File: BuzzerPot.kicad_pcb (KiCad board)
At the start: 2 copper layers, 29.9 x 15.1 mm, 9 parts, among them J1 ConnM_01x03_Horizontal_2.54mm, Q2 AO3400_C4748804

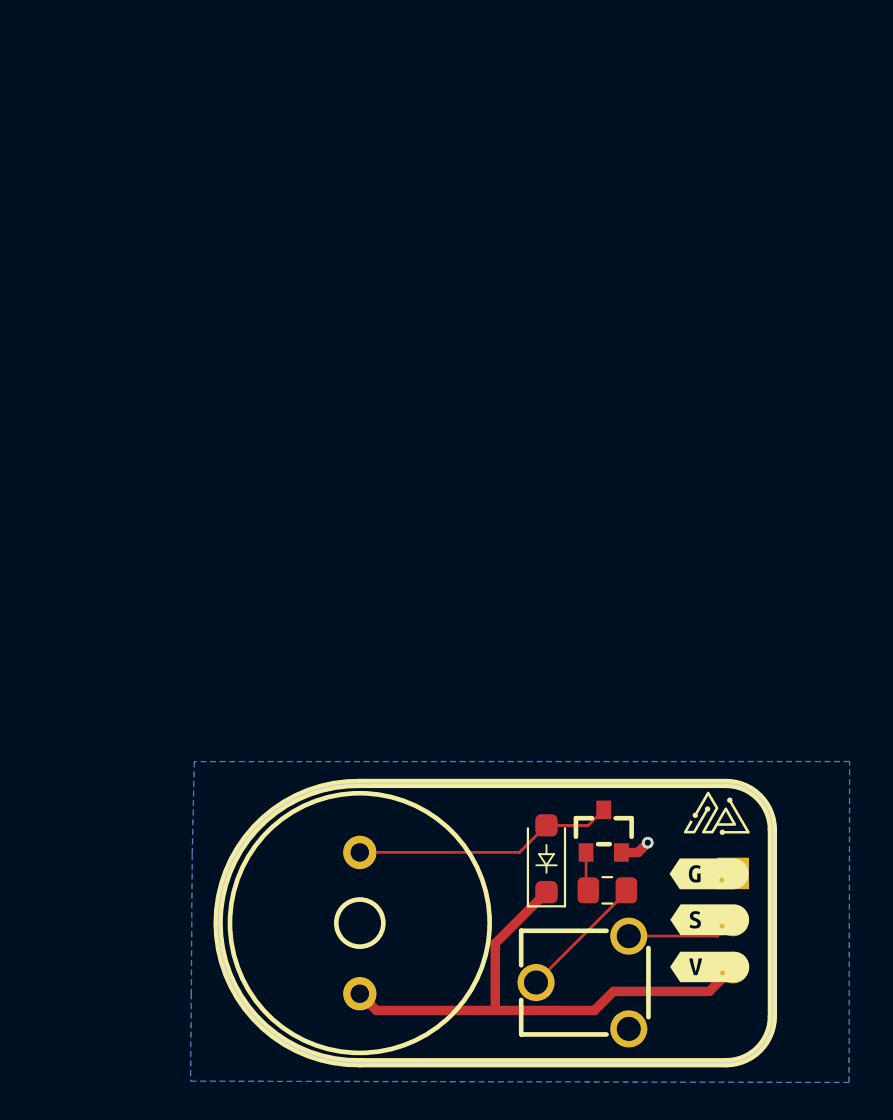
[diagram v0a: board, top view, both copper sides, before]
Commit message: Updated: Replaced Buzzer with Speaker
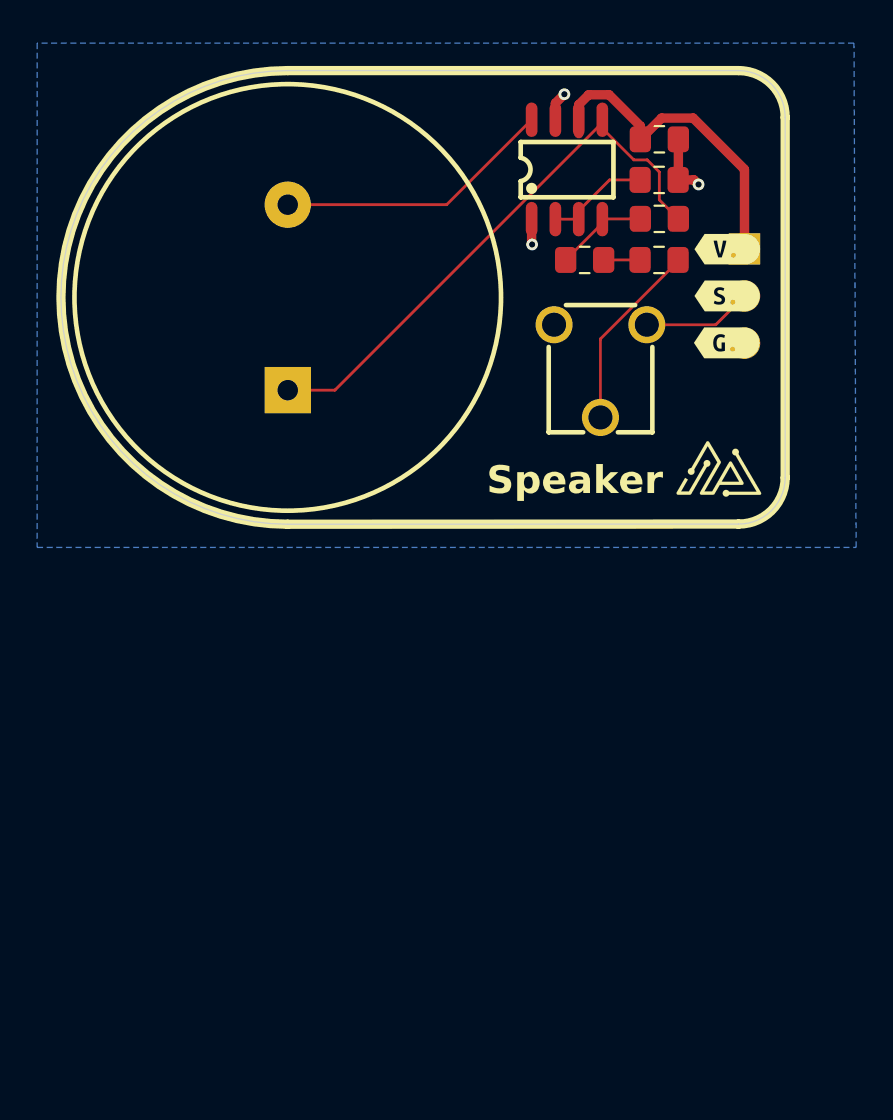
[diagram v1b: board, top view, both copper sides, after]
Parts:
- removed BUZZER2: SFN-1407PA7.6, easyeda2kicad:BUZ-TH_BD14.0-P7.60-D0.7
- removed D1: D_Schottky_SOD-123_xxV_xxA, Remal_KiCadLib:D_SOD-123
- removed Q2: AO3400_C4748804, easyeda2kicad:SOT-23_L2.9-W1.3-P1.90-LS2.4-BR
- removed kibuzzard-67C9871B: G***, kibuzzard-67C9871B
- removed kibuzzard-67C9872F: G***, kibuzzard-67C9872F
- removed kibuzzard-67C98740: G***, kibuzzard-67C98740
- added C1: 1uF, Remal_KiCadLib:C_0805_2012m, F.Cu at (156.4, 93.4)
- added C2: 1uF, Remal_KiCadLib:C_0805_2012m, F.Cu at (156.4, 91.2)
- added C3: 1uF, Remal_KiCadLib:C_0805_2012m, F.Cu at (156.4, 97.7)
- added R3: 20k, Remal_KiCadLib:R_0805_2012m, F.Cu at (156.4, 95.5)
- added SPK1: GSPK2307P-8R1W, easyeda2kicad:SPK-TH_BD23.0-P10.00-D0.8-L-RD, F.Cu at (136.4, 99.7)
- added U1: SC8002B, easyeda2kicad:SOP-8_L4.9-W3.9-P1.27-LS6.0-BL, F.Cu at (151.4, 92.8)
- added kibuzzard-67CEDACD: G***, kibuzzard-67CEDACD, F.Cu at (160.1, 99.7)
- added kibuzzard-67CEDAF1: G***, kibuzzard-67CEDAF1, F.Cu at (160.1, 102.2)
- added kibuzzard-67CEDAF9: G***, kibuzzard-67CEDAF9, F.Cu at (160.1, 97.1)
- R2: value 1k -> 20k
- moved R2 34.0 mm to (152.4, 97.7)
- moved J1 33.7 mm to (161.0, 97.1)
- moved R1 33.0 mm to (153.2, 103.7), turned to 180 degrees
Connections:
- J1 pad 1: GND -> +5V
- J1 pad 3: +5V -> GND
- R1 pad 1: GND -> SIG
- R1 pad 2: SIG -> GND
- R1 pad 3: Base -> Net-(C3-Pad1)
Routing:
- net Net-(SPK1-+): track 0.00 -> 30.6 mm
- net Net-(SPK1--): track 0.00 -> 15.4 mm
- net Net-(D1-A): track 14.1 -> 0.00 mm
- net Net-(C3-Pad1): track 0.00 -> 10.2 mm
- net +5V: track 29.0 -> 19.1 mm
- net Net-(U1-+IN): track 0.00 -> 5.71 mm
- net Base: track 6.99 -> 1.96 mm
- net GND: track 1.64 -> 6.35 mm, vias 1 -> 3
- net Net-(U1--IN): track 2.09 -> 5.33 mm
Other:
- board size 29.9 x 15.1 mm -> 39.1 x 24.5 mm
- board text added: "Speaker"

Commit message: Updated Version 2
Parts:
- removed R1: WH06-2C-103(10K), easyeda2kicad:RES-ADJ-TH_WH06-2C-103
- added H1: MountingHole_3.2mm_M3_NoConn, Remal_KiCadLib:MountingHole_3.2mm_M3_NoConn, F.Cu at (151.2, 99.7)
- added R4: WH06-2C-103(10K), easyeda2kicad:RES-ADJ-TH_WH06-2C-103, F.Cu at (152.2, 107.9)
- C3: footprint Remal_KiCadLib:C_0805_2012m -> Remal_KiCadLib:C_0402_1005m
- R2: footprint Remal_KiCadLib:R_0805_2012m -> Remal_KiCadLib:R_0402_1005m
- moved R3 9.72 mm to (149.1, 89.1), turned to 180 degrees
- moved R2 9.01 mm to (157.3, 90.2), turned to 90 degrees
- moved C2 7.63 mm to (149.1, 93.4), turned to 180 degrees
- moved C1 7.61 mm to (149.1, 91.2), turned to 0 degrees
- moved C3 5.07 mm to (157.3, 92.7), turned to 90 degrees
- moved J1 4.56 mm to (156.4, 97.2)
- moved kibuzzard-67CEDACD 4.56 mm to (155.5, 99.8)
- moved kibuzzard-67CEDAF1 4.56 mm to (155.5, 102.3)
- moved kibuzzard-67CEDAF9 4.56 mm to (155.5, 97.2)
- moved U1 2.81 mm to (153.9, 91.5), turned to 180 degrees
- turned SPK1 to -90 degrees
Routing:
- net Net-(SPK1-+): track 30.6 -> 21.7 mm
- net Net-(SPK1--): track 15.4 -> 23.9 mm
- net Net-(C3-Pad1): track 10.2 -> 15.8 mm
- net +5V: track 19.1 -> 13.6 mm
- net Net-(U1--IN): track 5.33 -> 9.31 mm
- net SIG: track 5.91 -> 9.16 mm
- net Base: track 1.96 -> 1.42 mm
- net GND: track 6.35 -> 5.81 mm
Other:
- board size 39.1 x 24.5 mm -> 34.9 x 25.2 mm
- board text removed: "Speaker"

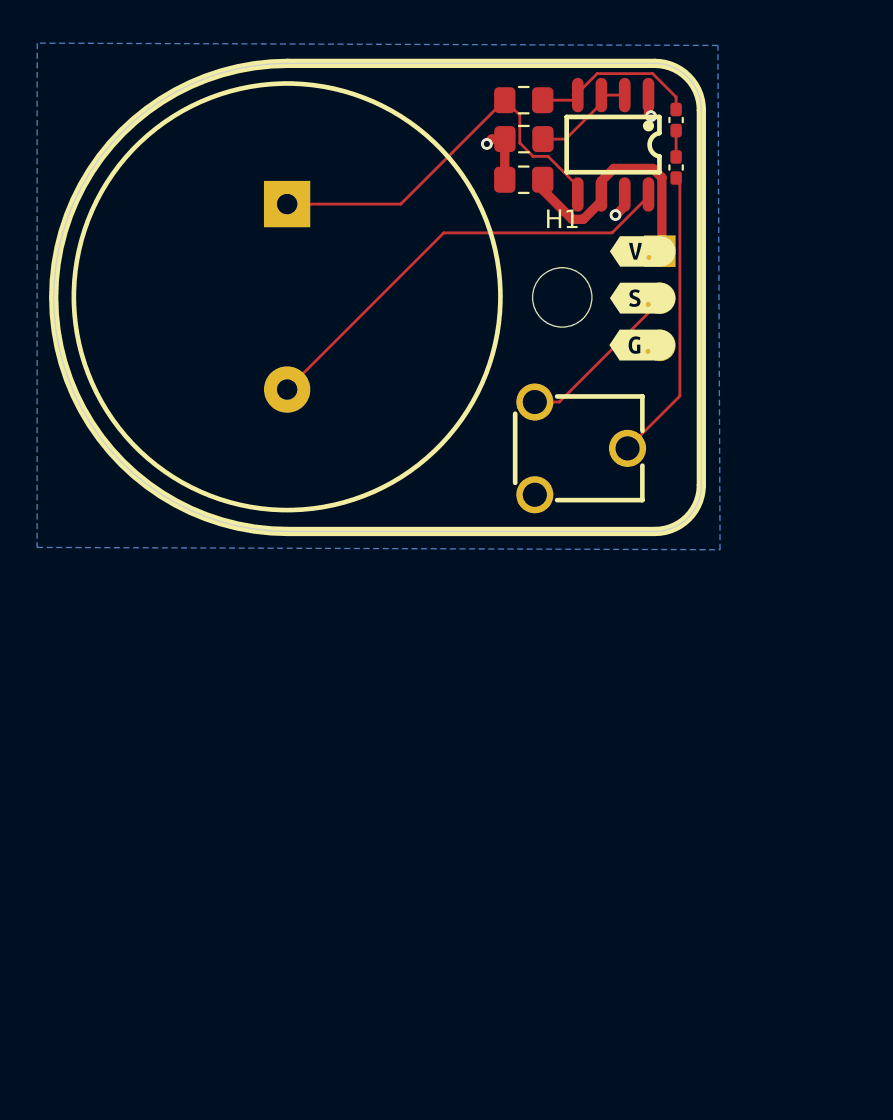
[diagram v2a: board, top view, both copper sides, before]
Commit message: Last Changes: Added Logo and Name
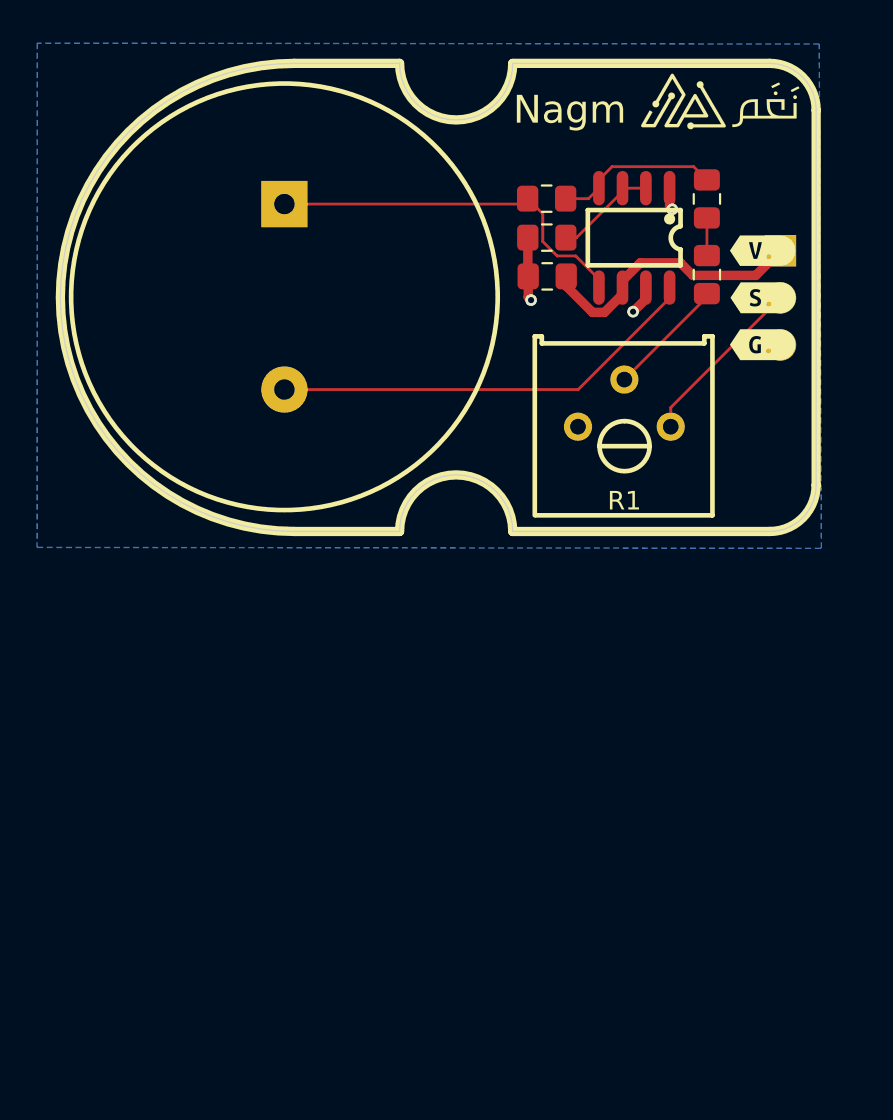
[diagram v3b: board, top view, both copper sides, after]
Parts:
- removed H1: MountingHole_3.2mm_M3_NoConn, Remal_KiCadLib:MountingHole_3.2mm_M3_NoConn
- removed R4: WH06-2C-103(10K), easyeda2kicad:RES-ADJ-TH_WH06-2C-103
- removed kibuzzard-67CEDAF9: G***, kibuzzard-67CEDAF9
- added G***: LOGO, practice_logo:nagm board, F.Cu at (162.1, 89.3)
- added R1: 3386P-1-103_C330583, easyeda2kicad:RES-ADJ-TH_3P-L9.5-W9.5-P2.50-L_3386P, F.Cu at (154.5, 105.4)
- added kibuzzard-67D2B7CA: G***, kibuzzard-67D2B7CA, F.Cu at (162.0, 97.2)
- C3: value 1uF -> 0.39uF; footprint Remal_KiCadLib:C_0402_1005m -> Remal_KiCadLib:C_0805_2012m
- R2: footprint Remal_KiCadLib:R_0402_1005m -> Remal_KiCadLib:R_0805_2012m
- moved J1 6.50 mm to (162.9, 97.2)
- moved kibuzzard-67CEDACD 6.50 mm to (162.0, 99.8)
- moved kibuzzard-67CEDAF1 6.50 mm to (162.0, 102.3)
- moved C3 6.01 mm to (159.0, 98.5)
- moved R3 5.45 mm to (150.3, 94.4)
- moved C1 5.45 mm to (150.3, 96.5), turned to 180 degrees
- moved C2 5.36 mm to (150.4, 98.6), turned to 0 degrees
- moved U1 5.15 mm to (155.1, 96.5)
- moved R2 4.57 mm to (159.0, 94.4)
- moved SPK1 0.15 mm to (136.2, 99.7)
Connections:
- C1 pad 1: GND -> Net-(U1-+IN)
- C1 pad 2: Net-(U1-+IN) -> GND
- C2 pad 1: +5V -> GND
- C2 pad 2: GND -> +5V
- C3 pad 1: Net-(C3-Pad1) -> Base
- C3 pad 2: Base -> Net-(C3-Pad2)
- R2 pad 1: Base -> Net-(C3-Pad2)
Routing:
- net Net-(C3-Pad1): track 15.8 -> 0.00 mm
- net Base: track 1.42 -> 6.65 mm
- net Net-(C3-Pad2): track 0.00 -> 2.03 mm
- net Net-(SPK1-+): track 21.7 -> 20.2 mm
- net +5V: track 13.6 -> 15.0 mm
- net Net-(SPK1--): track 23.9 -> 23.4 mm
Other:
- board size 34.9 x 25.2 mm -> 40.7 x 25.2 mm
- board text added: "Nagm"

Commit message: Updated: Remal Golden Standard Recheck
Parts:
- added G***: LOGO, practice_logo:remal_logo_big, B.Cu at (144.9, 99.7)
- added G***: LOGO, practice_logo:nagm board, B.Cu at (150.8, 88.7)
- added R4: 47k, Remal_KiCadLib:R_0805_2012m, F.Cu at (162.2, 93.8)
- added kibuzzard-67D32B23: G***, kibuzzard-67D32B23, B.Cu at (162.0, 97.2)
- added kibuzzard-67D32B2A: G***, kibuzzard-67D32B2A, B.Cu at (162.0, 99.8)
- added kibuzzard-67D32B2F: G***, kibuzzard-67D32B2F, B.Cu at (162.0, 102.3)
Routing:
- net +5V: track 15.0 -> 18.9 mm
- net GND: track 6.23 -> 7.90 mm, vias 3 -> 4
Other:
- board text added: "www.remal.io"

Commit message: Last Update: Inserted two Mounting Holes M2
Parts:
- added H1: MountingHole_2.2mm_M2_NoConn, Remal_KiCadLib:MountingHole_2.2mm_M2_NoConn, F.Cu at (146.1, 109.8)
- added H2: MountingHole_2.2mm_M2_NoConn, Remal_KiCadLib:MountingHole_2.2mm_M2_NoConn, F.Cu at (146.1, 89.6)
- moved G*** 0.91 mm to (150.3, 89.5)
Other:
- outline, holes or cut-outs redrawn
